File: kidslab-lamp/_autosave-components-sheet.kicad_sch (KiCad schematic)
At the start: 25 parts, among them J1 HY-4A, J2 pin_header_1x3, J3 pin_header_1x3, U2 LSM6DS3

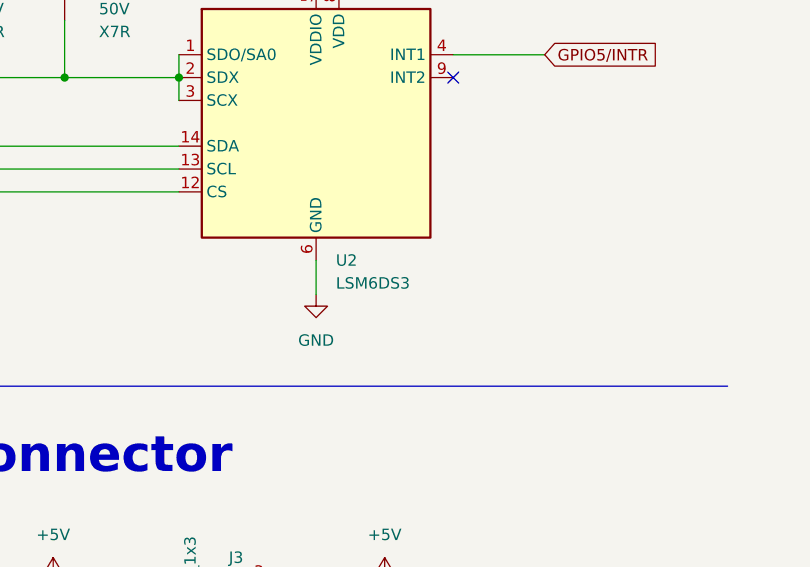
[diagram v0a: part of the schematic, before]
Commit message: adding coordinate system for imu, changing imu part, changing touch resitros to pull down
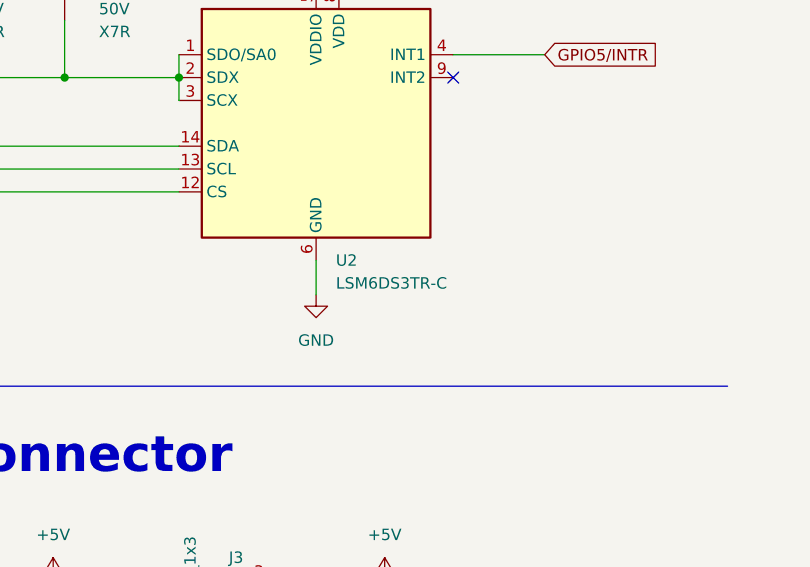
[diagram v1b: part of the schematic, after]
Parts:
- U2: value LSM6DS3 -> LSM6DS3TR-C; LCSC Part # C95230 -> C967633
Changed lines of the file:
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@@
       (effects (font (size 1.27 1.27)) (justify left))
     )
-    (property "Value" "LSM6DS3" (at 174.9141 69.85 0)
+    (property "Value" "LSM6DS3TR-C" (at 174.9141 69.85 0)
       (effects (font (size 1.27 1.27)) (justify left))
     )
@@
       (effects (font (size 1.27 1.27)) hide)
     )
-    (property "LCSC Part #" "C95230" (at 172.72 52.07 0)
+    (property "LCSC Part #" "C967633" (at 172.72 52.07 0)
       (effects (font (size 1.27 1.27)) hide)
     )
